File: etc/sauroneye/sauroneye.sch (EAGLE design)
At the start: 7 parts

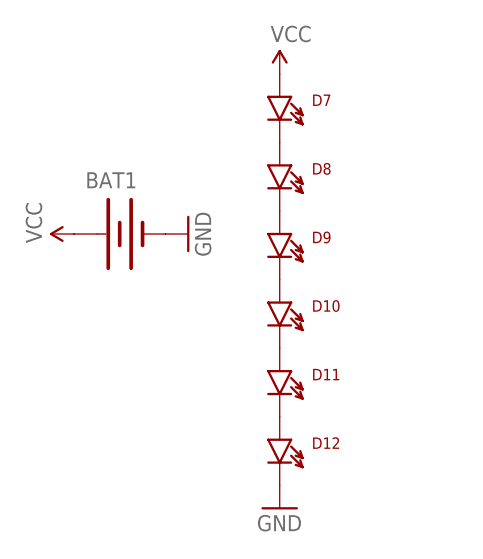
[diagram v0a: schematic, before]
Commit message: update to board
  * board now obeys physics and laws of electricity
  * board has USB connector
  * removing whatever those spurious eagle files are and ignoring them
    in the future
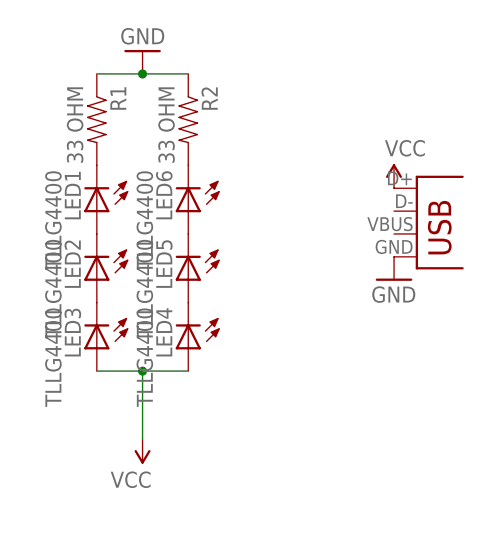
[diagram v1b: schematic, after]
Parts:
- removed BAT1: (no value), SparkFun-Electromechanical:BATTERY12PTH
- removed D10, D11, D12, D7, D8, D9: (no value), SparkFun-LED:LTE-302
- added LED1, LED2, LED3, LED4, LED5, LED6: TLLG4400, led:TLLG4400
- added R1, R2: 33 OHM, SparkFun:RESISTORAXIAL-0.3
- added X1: USBSMD, SparkFun:USBSMD
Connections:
- removed net N$10: D11.C, D12.A
- removed net N$7: D8.C, D9.A
- removed net N$8: D10.A, D9.C
- removed net N$9: D10.C, D11.A
- new net N$1: LED6.C, R2.2
- new net N$2: LED1.C, R1.2
- new net N$3: LED5.C, LED6.A
- new net N$4: LED4.C, LED5.A
- new net N$5: LED1.A, LED2.C
- net GND: now also R1.1, R2.1, X1.GND; no longer BAT1.-, D12.C
- net N$6: now also LED2.A, LED3.C; no longer D7.C, D8.A
- net VCC: now also LED3.A, LED4.A, X1.D+; no longer BAT1.+, D7.A
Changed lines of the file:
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@@
 <?xml version="1.0" encoding="utf-8"?>
 <!DOCTYPE eagle SYSTEM "eagle.dtd">
-<eagle version="6.3">
+<eagle version="6.2">
 <drawing>
 <settings>
@@
 </classes>
 <parts>
-<part name="D7" library="SparkFun-LED" deviceset="LTE-302" device=""/>
-<part name="D8" library="SparkFun-LED" deviceset="LTE-302" device=""/>
-<part name="D9" library="SparkFun-LED" deviceset="LTE-302" device=""/>
-<part name="D10" library="SparkFun-LED" deviceset="LTE-302" device=""/>
-<part name="D11" library="SparkFun-LED" deviceset="LTE-302" device=""/>
-<part name="D12" library="SparkFun-LED" deviceset="LTE-302" device=""/>
-<part name="BAT1" library="SparkFun-Electromechanical" deviceset="BATTERY" device="12PTH"/>
-<part name="P+1" library="SparkFun-Aesthetics" deviceset="VCC" device=""/>
-<part name="P+2" library="SparkFun-Aesthetics" deviceset="VCC" device=""/>
-<part name="GND1" library="SparkFun-Aesthetics" deviceset="GND" device=""/>
-<part name="GND2" library="SparkFun-Aesthetics" deviceset="GND" device=""/>
+<part name="X1" library="SparkFun" deviceset="USB" device="SMD"/>
+<part name="P+1" library="SparkFun" deviceset="VCC" device=""/>
+<part name="P+2" library="SparkFun" deviceset="VCC" device=""/>
+<part name="GND1" library="SparkFun" deviceset="GND" device=""/>
+<part name="GND2" library="SparkFun" deviceset="GND" device=""/>
+<part name="LED1" library="led" deviceset="TLLG4400" device=""/>
+<part name="LED2" library="led" deviceset="TLLG4400" device=""/>
+<part name="LED3" library="led" deviceset="TLLG4400" device=""/>
+<part name="LED4" library="led" deviceset="TLLG4400" device=""/>
+<part name="LED5" library="led" deviceset="TLLG4400" device=""/>
+<part name="LED6" library="led" deviceset="TLLG4400" device=""/>
+<part name="R1" library="SparkFun" deviceset="RESISTOR" device="AXIAL-0.3" value="33 OHM"/>
+<part name="R2" library="SparkFun" deviceset="RESISTOR" device="AXIAL-0.3" value="33 OHM"/>
 </parts>
 <sheets>
@@
 </plain>
 <instances>
-<instance part="D7" gate="G$1" x="40.64" y="81.28"/>
-<instance part="D8" gate="G$1" x="40.64" y="73.66"/>
-<instance part="D9" gate="G$1" x="40.64" y="66.04"/>
-<instance part="D10" gate="G$1" x="40.64" y="58.42"/>
-<instance part="D11" gate="G$1" x="40.64" y="50.8"/>
-<instance part="D12" gate="G$1" x="40.64" y="43.18"/>
-<instance part="BAT1" gate="G$1" x="22.86" y="66.04"/>
-<instance part="P+1" gate="1" x="40.64" y="83.82"/>
-<instance part="P+2" gate="1" x="17.78" y="66.04" rot="R90"/>
-<instance part="GND1" gate="1" x="40.64" y="35.56"/>
-<instance part="GND2" gate="1" x="30.48" y="66.04" rot="R90"/>
+<instance part="X1" gate="G$1" x="55.88" y="63.5"/>
+<instance part="P+1" gate="1" x="53.34" y="71.12"/>
+<instance part="P+2" gate="1" x="25.4" y="43.18" rot="R180"/>
+<instance part="GND1" gate="1" x="25.4" y="86.36" rot="R180"/>
+<instance part="GND2" gate="1" x="53.34" y="60.96"/>
+<instance part="LED1" gate="G$1" x="20.32" y="68.58" rot="R180"/>
+<instance part="LED2" gate="G$1" x="20.32" y="60.96" rot="R180"/>
+<instance part="LED3" gate="G$1" x="20.32" y="53.34" rot="R180"/>
+<instance part="LED4" gate="G$1" x="30.48" y="53.34" rot="R180"/>
+<instance part="LED5" gate="G$1" x="30.48" y="60.96" rot="R180"/>
+<instance part="LED6" gate="G$1" x="30.48" y="68.58" rot="R180"/>
+<instance part="R1" gate="G$1" x="20.32" y="78.74" rot="R270"/>
+<instance part="R2" gate="G$1" x="30.48" y="78.74" rot="R270"/>
 </instances>
 <busses>
 </busses>
 <nets>
+<net name="VCC" class="0">
+<segment>
+<pinref part="X1" gate="G$1" pin="D+"/>
+<pinref part="P+1" gate="1" pin="VCC"/>
+</segment>
+<segment>
+<pinref part="LED3" gate="G$1" pin="A"/>
+<pinref part="P+2" gate="1" pin="VCC"/>
+<wire x1="20.32" y1="50.8" x2="25.4" y2="50.8" width="0.2032" layer="91"/>
+<wire x1="25.4" y1="50.8" x2="25.4" y2="43.18" width="0.2032" layer="91"/>
+<pinref part="LED4" gate="G$1" pin="A"/>
+<wire x1="30.48" y1="50.8" x2="25.4" y2="50.8" width="0.2032" layer="91"/>
+<junction x="25.4" y="50.8"/>
+</segment>
+</net>
+<net name="GND" class="0">
+<segment>
+<pinref part="X1" gate="G$1" pin="GND"/>
+<pinref part="GND2" gate="1" pin="GND"/>
+</segment>
+<segment>
+<pinref part="R1" gate="G$1" pin="1"/>
+<pinref part="GND1" gate="1" pin="GND"/>
+<wire x1="20.32" y1="83.82" x2="25.4" y2="83.82" width="0.2032" layer="91"/>
+<pinref part="R2" gate="G$1" pin="1"/>
+<wire x1="25.4" y1="83.82" x2="30.48" y2="83.82" width="0.2032" layer="91"/>
+<junction x="25.4" y="83.82"/>
+</segment>
+</net>
+<net name="N$1" class="0">
+<segment>
+<pinref part="R2" gate="G$1" pin="2"/>
+<pinref part="LED6" gate="G$1" pin="C"/>
+</segment>
+</net>
+<net name="N$2" class="0">
+<segment>
+<pinref part="R1" gate="G$1" pin="2"/>
+<pinref part="LED1" gate="G$1" pin="C"/>
+</segment>
+</net>
+<net name="N$3" class="0">
+<segment>
+<pinref part="LED6" gate="G$1" pin="A"/>
+<pinref part="LED5" gate="G$1" pin="C"/>
+</segment>
+</net>
+<net name="N$4" class="0">
+<segment>
+<pinref part="LED5" gate="G$1" pin="A"/>
+<pinref part="LED4" gate="G$1" pin="C"/>
+</segment>
+</net>
+<net name="N$5" class="0">
+<segment>
+<pinref part="LED1" gate="G$1" pin="A"/>
+<pinref part="LED2" gate="G$1" pin="C"/>
+</segment>
+</net>
 <net name="N$6" class="0">
 <segment>
-<pinref part="D7" gate="G$1" pin="C"/>
-<pinref part="D8" gate="G$1" pin="A"/>
-</segment>
-</net>
-<net name="N$7" class="0">
-<segment>
-<pinref part="D8" gate="G$1" pin="C"/>
-<pinref part="D9" gate="G$1" pin="A"/>
-</segment>
-</net>
-<net name="N$8" class="0">
-<segment>
-<pinref part="D9" gate="G$1" pin="C"/>
-<pinref part="D10" gate="G$1" pin="A"/>
-</segment>
-</net>
-<net name="N$9" class="0">
-<segment>
-<pinref part="D10" gate="G$1" pin="C"/>
-<pinref part="D11" gate="G$1" pin="A"/>
-</segment>
-</net>
-<net name="N$10" class="0">
-<segment>
-<pinref part="D11" gate="G$1" pin="C"/>
-<pinref part="D12" gate="G$1" pin="A"/>
-</segment>
-</net>
-<net name="VCC" class="0">
-<segment>
-<pinref part="D7" gate="G$1" pin="A"/>
-<pinref part="P+1" gate="1" pin="VCC"/>
-</segment>
-<segment>
-<pinref part="BAT1" gate="G$1" pin="+"/>
-<pinref part="P+2" gate="1" pin="VCC"/>
-</segment>
-</net>
-<net name="GND" class="0">
-<segment>
-<pinref part="D12" gate="G$1" pin="C"/>
-<pinref part="GND1" gate="1" pin="GND"/>
-</segment>
-<segment>
-<pinref part="BAT1" gate="G$1" pin="-"/>
-<pinref part="GND2" gate="1" pin="GND"/>
-</segment>
-</net>
+<pinref part="LED2" gate="G$1" pin="A"/>
+<pinref part="LED3" gate="G$1" pin="C"/>
+</segment>
+</net>

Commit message: sauroneye board bugfixing
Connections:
- net VCC: now also X1.VBUS; no longer X1.D+
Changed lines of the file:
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@@
 <instances>
 <instance part="X1" gate="G$1" x="55.88" y="63.5"/>
-<instance part="P+1" gate="1" x="53.34" y="71.12"/>
+<instance part="P+1" gate="1" x="50.8" y="66.04" rot="R90"/>
 <instance part="P+2" gate="1" x="25.4" y="43.18" rot="R180"/>
 <instance part="GND1" gate="1" x="25.4" y="86.36" rot="R180"/>
@@
 <net name="VCC" class="0">
 <segment>
-<pinref part="X1" gate="G$1" pin="D+"/>
-<pinref part="P+1" gate="1" pin="VCC"/>
-</segment>
-<segment>
 <pinref part="LED3" gate="G$1" pin="A"/>
 <pinref part="P+2" gate="1" pin="VCC"/>
@@
 <junction x="25.4" y="50.8"/>
 </segment>
+<segment>
+<pinref part="X1" gate="G$1" pin="VBUS"/>
+<pinref part="P+1" gate="1" pin="VCC"/>
+<wire x1="50.8" y1="66.04" x2="53.34" y2="66.04" width="0.1524" layer="91"/>
+</segment>
 </net>

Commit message: new design files from Mark Oehlberg
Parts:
- removed X1: USBSMD, SparkFun:USBSMD
- added JP1: (no value), SparkFun-Connectors:M02PTH
- added LED7, LED8: (no value), adafruit:LEDCHIP-LED0805
- added R3, R4, R5, R6, R7, R8: 100, adafruit:R-US_R0805
- LED1, LED2, LED3, LED4, LED5, LED6: value TLLG4400 -> (none); device led:TLLG4400 -> adafruit:LEDCHIP-LED0805
- R1, R2: value 33 OHM -> 100; device SparkFun:RESISTORAXIAL-0.3 -> adafruit:R-US_R0805
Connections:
- removed net GND: R1.1, R2.1, X1.GND
- removed net VCC: LED3.A, LED4.A, X1.VBUS
- new net N$10: LED8.A, R8.1
- new net N$7: LED2.A, R5.1
- new net N$8: LED4.A, R6.1
- new net N$9: LED6.A, R7.1
- net N$1: now also JP1.2, R1.2, R3.2, R4.2, R5.2, R6.2, R7.2, R8.2; no longer LED6.C
- net N$2: now also LED1.A, R1.1; no longer LED1.C, R1.2
- net N$3: now also LED3.A, R2.1; no longer LED5.C, LED6.A
- net N$4: now also R3.1; no longer LED4.C
- net N$5: now also LED7.A, R4.1; no longer LED1.A, LED2.C
- net N$6: now also JP1.1, LED1.C, LED2.C, LED4.C, LED5.C, LED6.C, LED7.C, LED8.C; no longer LED2.A
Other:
- moved on the sheet: LED1, LED2, LED3, LED4, LED5, LED6, R1, R2
